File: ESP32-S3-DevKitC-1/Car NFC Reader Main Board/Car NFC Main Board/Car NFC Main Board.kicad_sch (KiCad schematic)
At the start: 2 parts

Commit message: Final submitted version
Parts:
- added J1: ~, symbol David_Library:YK441
- added SW1, SW2: SW_SPDT, Button_Switch_THT:SW_CuK_OS102011MA1QN1_SPDT_Angled, symbol Switch:SW_SPDT
- added U1: ESP32-S3-DevKitC, PCM_Espressif:ESP32-S3-DevKitC, symbol PCM_Espressif:ESP32-S3-DevKitC
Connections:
- net +5V: now also J1.1 (Pin_1), U1.21 (5V)
- net GND: now also R2.2, J1.2 (Pin_2), J1.3 (Pin_3), SW1.2 (B), SW2.2 (B), U1.22 (GND), U1.23 (GND), U1.24 (GND), U1.44 (GND); no longer R2.1
- net at R1.2: now also R2.1, U1.16 (GPIO10/ADC1_CH9); no longer R2.2
- net +12V renamed DOME
- net DOME: now also J1.4 (Pin_4)
- new net: U1.1 (3V3), U1.2 (3V3)
- new net: SW2.1 (A), U1.40 (GPIO2/ADC1_CH1)
- new net: SW1.1 (A), U1.41 (GPIO1/ADC1_CH0)
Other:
- moved on the sheet: R1

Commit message: Gave new resistor values matching what's tested in the honda
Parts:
- R1: value 4.7K -> 470K
- R2: value 200R -> 33K
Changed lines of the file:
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@@
 			)
 		)
-		(property "Value" "200R"
+		(property "Value" "33K"
 			(at 128.27 88.9 90)
 			(effects
@@
 			)
 		)
-		(property "Value" "4.7K"
+		(property "Value" "470K"
 			(at 118.11 88.9 90)
 			(effects

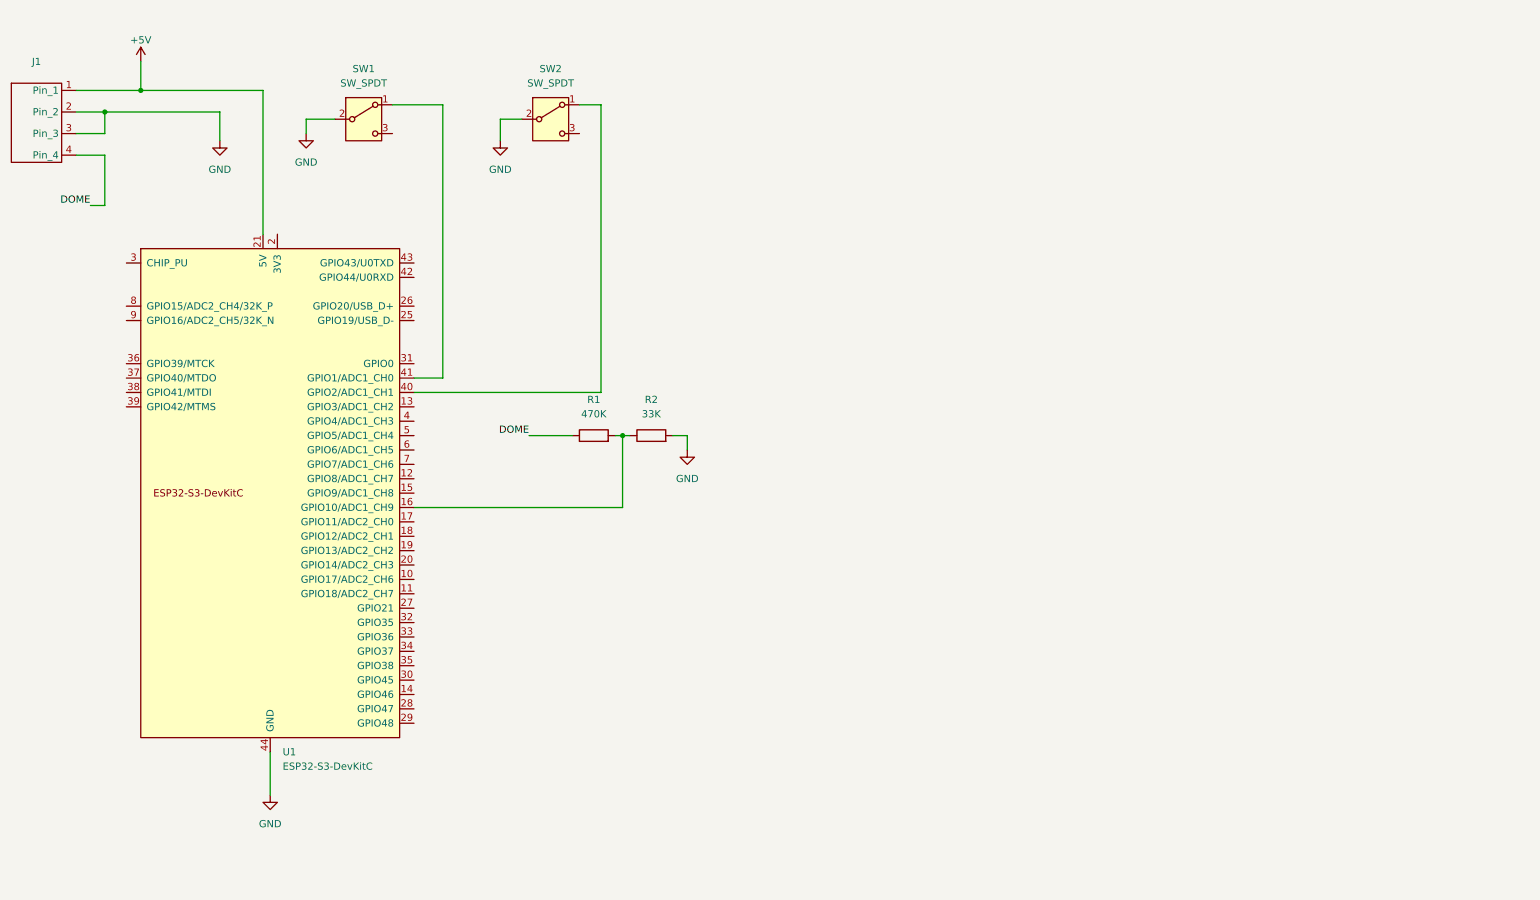
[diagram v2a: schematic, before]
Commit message: NFC reader board version submitted to JLCPCB
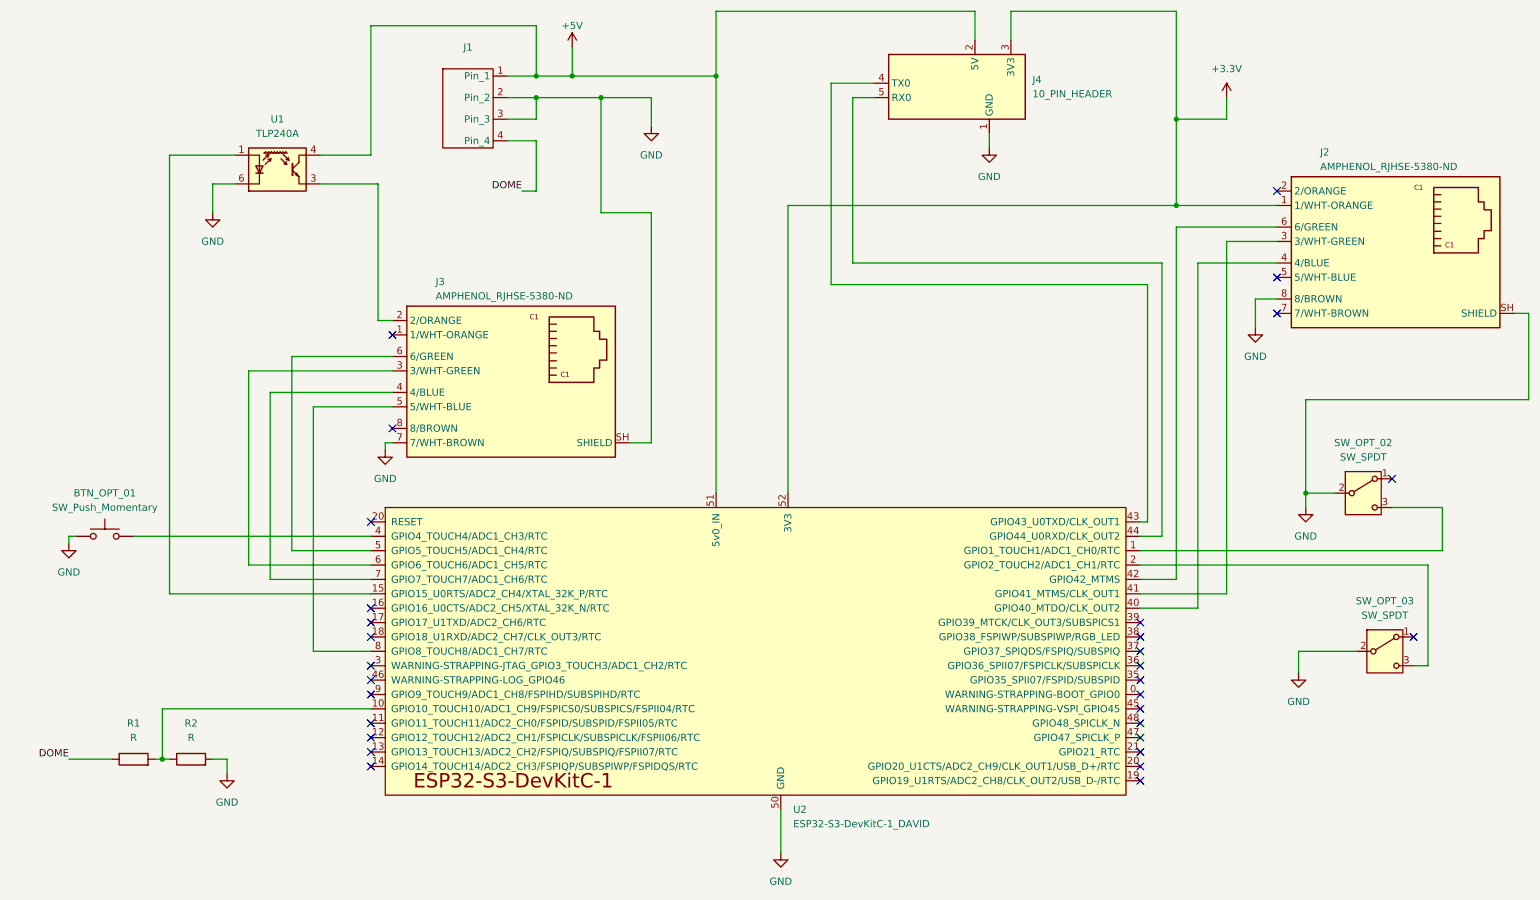
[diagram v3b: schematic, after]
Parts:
- removed U1: ESP32-S3-DevKitC, PCM_Espressif:ESP32-S3-DevKitC, symbol PCM_Espressif:ESP32-S3-DevKitC
- added BTN_OPT_01: SW_Push_Momentary, Footprint_Library:MOMENTARY_BUTTON, symbol David_Library:SW_Push_Momentary
- added J2, J3: AMPHENOL_RJHSE-5380-ND, Connector_RJ:RJ45_Amphenol_RJHSE5380, symbol David_Library:AMPHENOL_RJHSE-5380-ND
- added J4: 10_PIN_HEADER, Footprint_Library:8_PIN_HEADER, symbol David_Library:10_PIN_HEADER
- added U1: TLP240A, TLP240A, symbol David_Library:TLP240A
- added U2: ESP32-S3-DevKitC-1_DAVID, Footprint_Library:ESP32-S3-DEVKITC_DAVID, symbol David_Library:ESP32-S3-DevKitC-1_DAVID
- J1: footprint (none) -> Footprint_Library:YK441 Screw Terminal Block_CAR_NFC
- R1: value 470K -> R
- R2: value 33K -> R
- renumbered SW1 to SW_OPT_02, SW2 to SW_OPT_03
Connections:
- net +5V: now also J4.2 (5V), U1.4 (C), U2.51 (5v0_IN)
- net GND: now also BTN_OPT_01.1, J2.8 (8/BROWN), J2.SH (SHIELD), J3.7 (7/WHT-BROWN), J3.SH (SHIELD), J4.1 (GND), U1.6 (K), U2.50 (GND)
- net at R1.2, R2.1: now also U2.10 (GPIO10_TOUCH10/ADC1_CH9/FSPICS0/SUBSPICS/FSPII04/RTC)
- net at SW_OPT_03.3 (C): now also U2.2 (GPIO2_TOUCH2/ADC1_CH1/RTC)
- net at SW_OPT_02.3 (C): now also U2.1 (GPIO1_TOUCH1/ADC1_CH0/RTC)
- new net: U1.1 (A), U2.15 (GPIO15_U0RTS/ADC2_CH4/XTAL_32K_P/RTC)
- new net: J3.2 (2/ORANGE), U1.3 (E)
- new net: J3.3 (3/WHT-GREEN), U2.6 (GPIO6_TOUCH6/ADC1_CH5/RTC)
- new net: J3.4 (4/BLUE), U2.7 (GPIO7_TOUCH7/ADC1_CH6/RTC)
- new net: J3.5 (5/WHT-BLUE), U2.8 (GPIO8_TOUCH8/ADC1_CH7/RTC)
- new net: J3.6 (6/GREEN), U2.5 (GPIO5_TOUCH5/ADC1_CH4/RTC)
- new net: J2.3 (3/WHT-GREEN), U2.41 (GPIO41_MTMS/CLK_OUT1)
- new net: J2.4 (4/BLUE), U2.40 (GPIO40_MTDO/CLK_OUT2)
- new net: J2.6 (6/GREEN), U2.42 (GPIO42_MTMS)
- new net: BTN_OPT_01.2, U2.4 (GPIO4_TOUCH4/ADC1_CH3/RTC)
- new net: J4.4 (TX0), U2.43 (GPIO43_U0TXD/CLK_OUT1)
- new net: J4.5 (RX0), U2.44 (GPIO44_U0RXD/CLK_OUT2)
- new net +3.3V: J2.1 (1/WHT-ORANGE), J4.3 (3V3), U2.52 (3V3)
- no-connect marks 0 -> 30
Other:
- moved on the sheet: J1, R1, R2, SW_OPT_02, SW_OPT_03

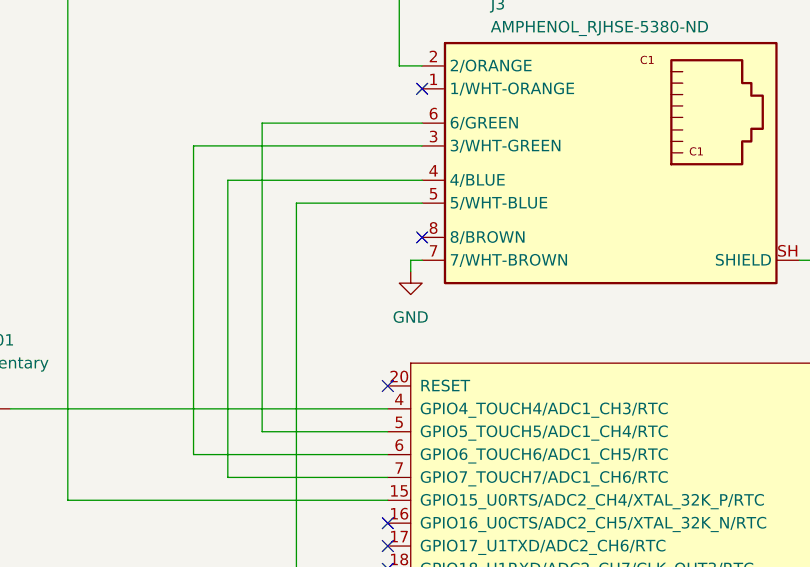
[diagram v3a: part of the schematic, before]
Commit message: Fixed PCB and schematic where GND pin on NFC reader ethernet port went to pin 7 instead of pin 8 like it should have
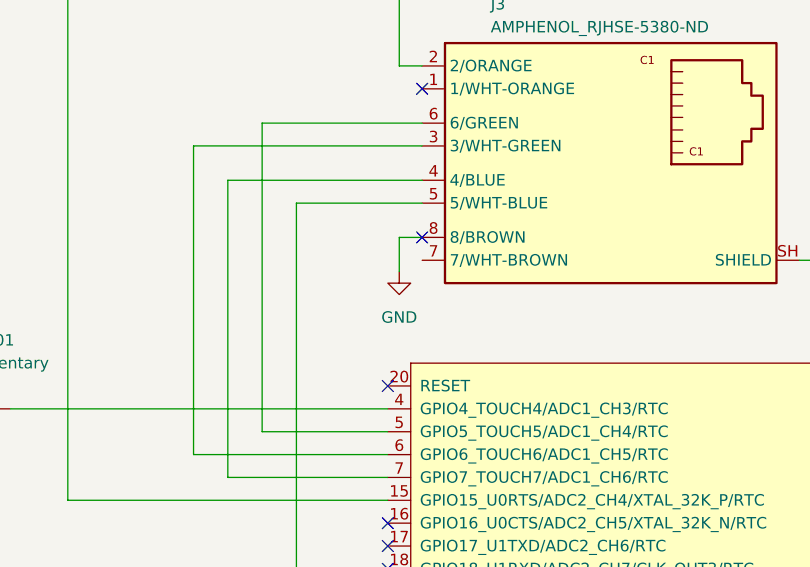
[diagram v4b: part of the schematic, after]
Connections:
- net GND: now also J3.8 (8/BROWN); no longer J3.7 (7/WHT-BROWN)
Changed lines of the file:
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@@
+	(wire
+		(pts
+			(xy 80.01 91.44) (xy 80.01 95.25)
+		)
+		(stroke
+			(width 0)
+			(type default)
+		)
+	)
 	(wire
 		(pts
@@
 	(wire
 		(pts
-			(xy 81.28 93.98) (xy 82.55 93.98)
+			(xy 80.01 91.44) (xy 82.55 91.44)
 		)
 		(stroke
@@
 		(pts
 			(xy 78.74 115.57) (xy 57.15 115.57)
-		)
-		(stroke
-			(width 0)
-			(type default)
-		)
-	)
-	(wire
-		(pts
-			(xy 81.28 95.25) (xy 81.28 93.98)
 		)
 		(stroke
@@
 	(symbol
 		(lib_id "power:GND")
-		(at 81.28 95.25 0)
+		(at 80.01 95.25 0)
 		(unit 1)
 		(exclude_from_sim no)
@@
 		(fields_autoplaced yes)
 		(property "Reference" "#PWR08"
-			(at 81.28 101.6 0)
+			(at 80.01 101.6 0)
 			(effects
 				(font
@@
 		)
 		(property "Value" "GND"
-			(at 81.28 100.33 0)
+			(at 80.01 100.33 0)
 			(effects
 				(font
@@
 		)
 		(property "Footprint" ""
-			(at 81.28 95.25 0)
+			(at 80.01 95.25 0)
 			(effects
 				(font
@@
 		)
 		(property "Datasheet" ""
-			(at 81.28 95.25 0)
+			(at 80.01 95.25 0)
 			(effects
 				(font
@@
 		)
 		(property "Description" "Power symbol creates a global label with name \"GND\" , ground"
-			(at 81.28 95.25 0)
-			(effects
-				(font
+			(at 80.01 95.25 0)
+			(effects
+				(font
